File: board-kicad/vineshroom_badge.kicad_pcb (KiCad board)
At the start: 2 copper layers, 95 x 95.7 mm, 74 parts, among them IC1 ATTINY20-X, P1 CONN_01X05, Q1 Q_NMOS_DGS

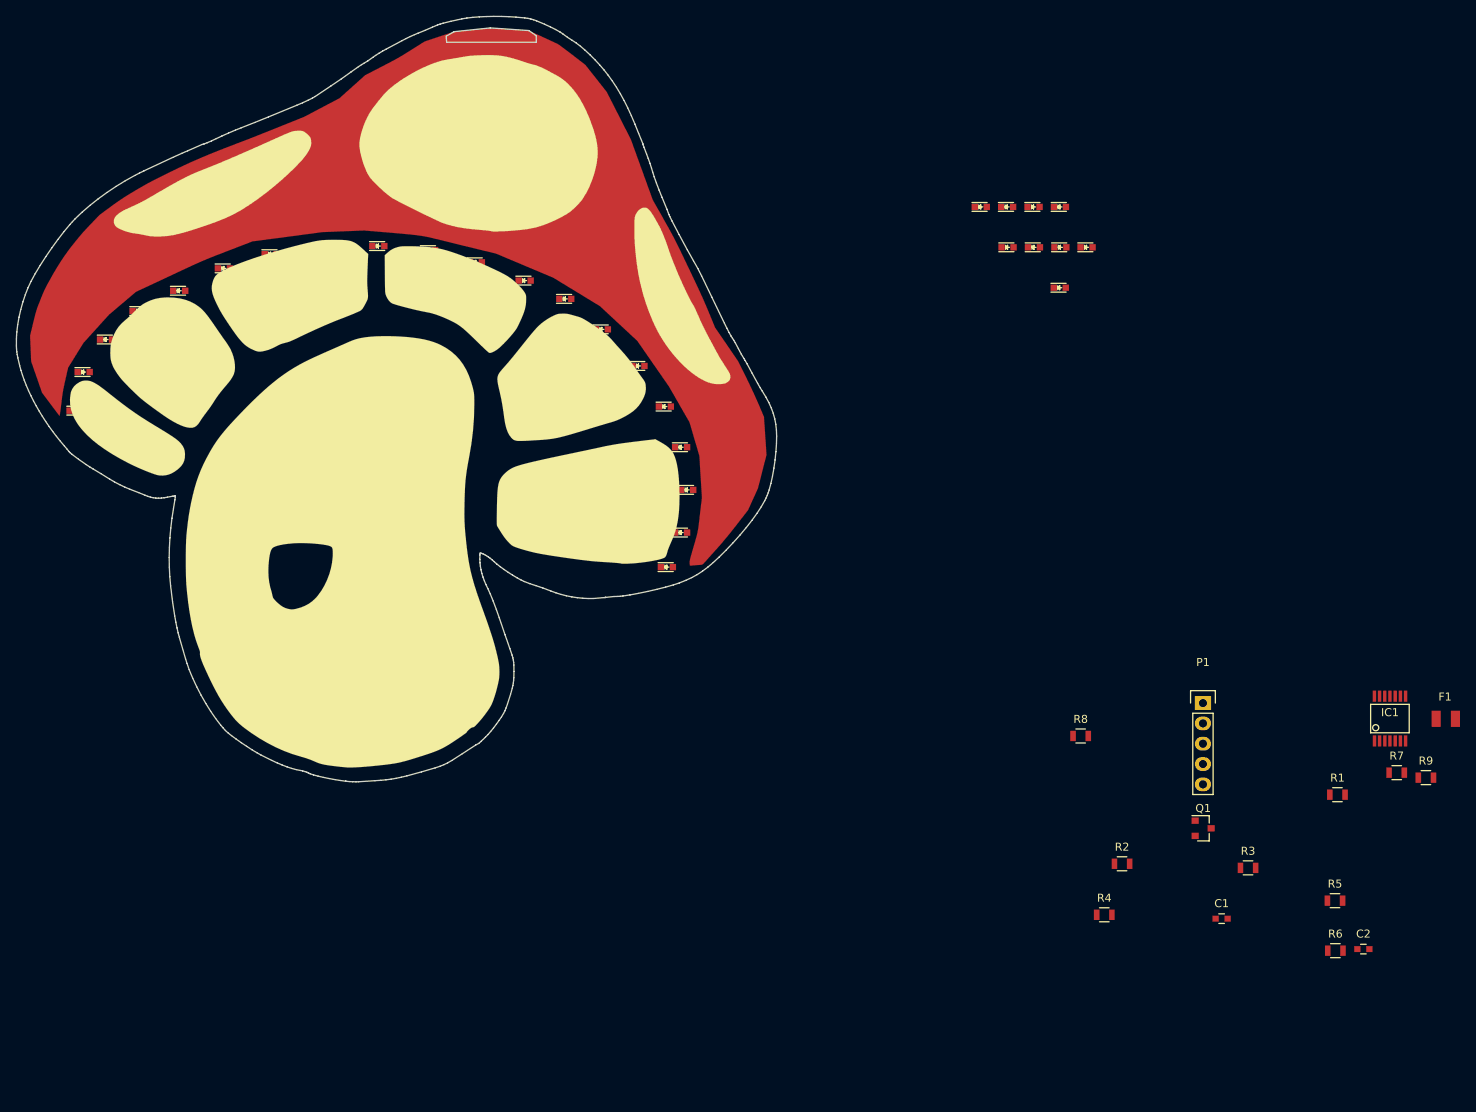
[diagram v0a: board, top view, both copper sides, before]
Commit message: starting LED placement
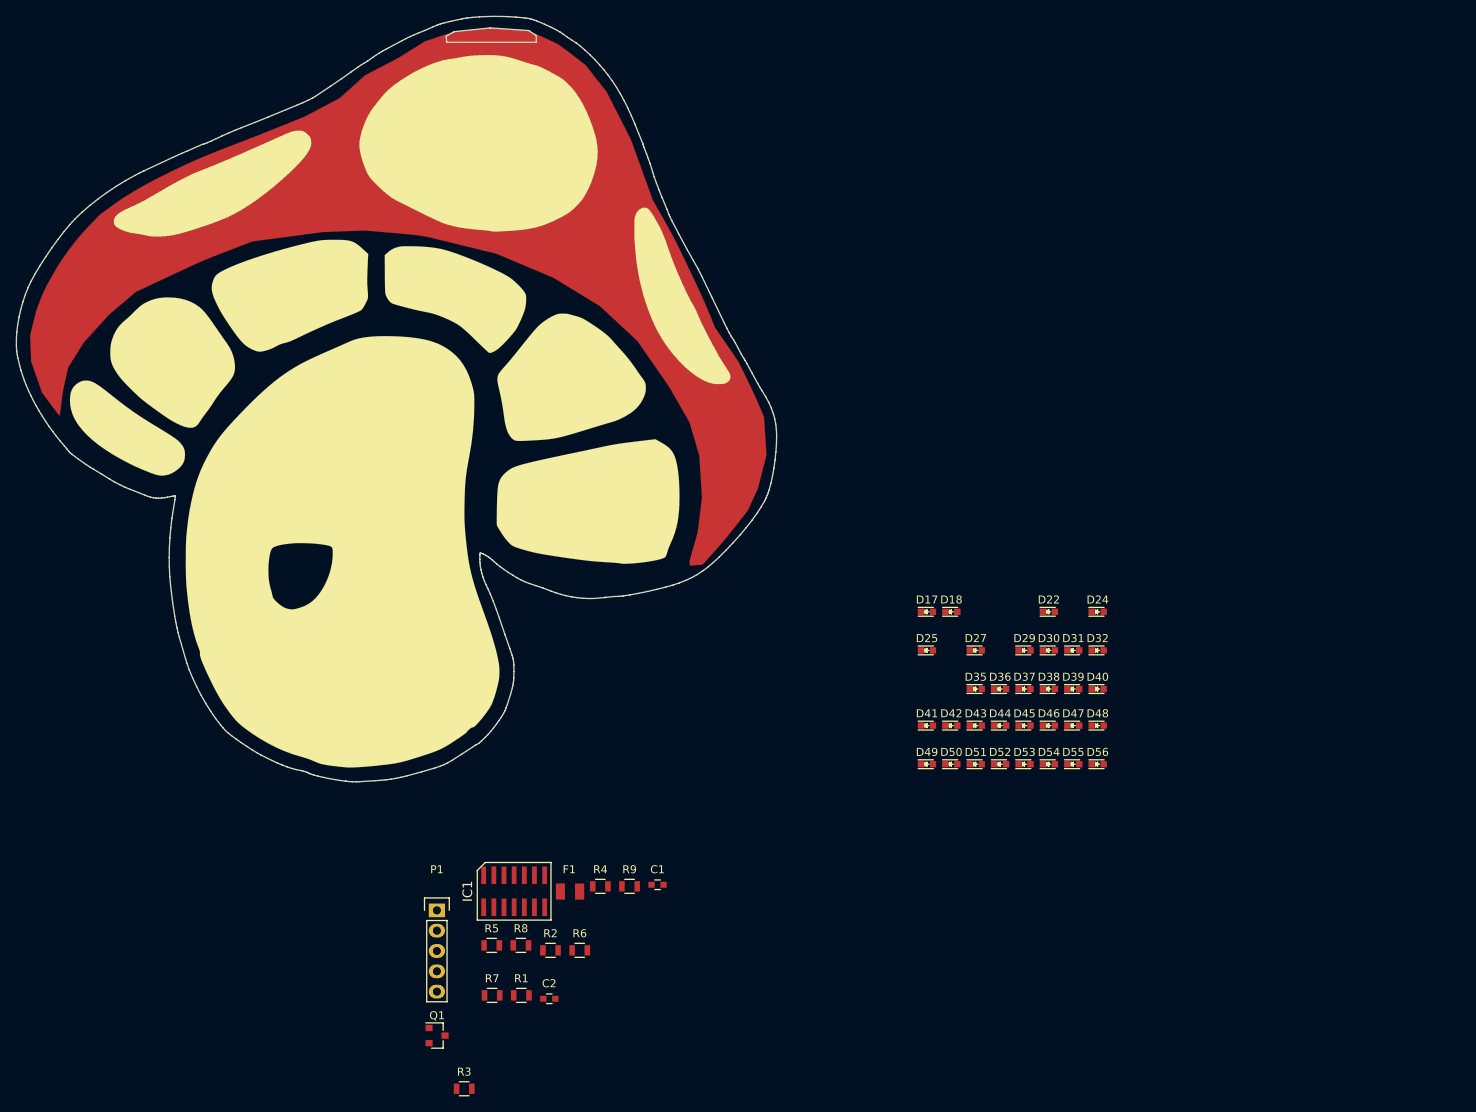
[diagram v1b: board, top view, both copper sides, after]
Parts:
- removed the G*** at (104.1, 75.7) (x3)
- added G*** (x2): LOGO, LOGO, F.Cu at (104.1, 75.7)
- added G***: LOGO, LOGO, F.Cu at (108.4, 160.3)
- IC1: footprint SMD_Packages:SSOP-14 -> spang_badge:ATTINY20_SOIC-14
- moved D48 134.2 mm to (193.3, 116.6)
- moved D24 125.6 mm to (193.3, 102.4)
- moved D22 124.2 mm to (187.2, 102.4)
- moved R7 116.5 mm to (117.6, 150.3)
- moved D55 113.5 mm to (190.2, 121.4)
- moved F1 111.6 mm to (127.3, 137.3)
- moved IC1 111.6 mm to (120.4, 137.3)
- moved D18 111.0 mm to (175.0, 102.4)
- moved D27 109.2 mm to (178.1, 107.2)
- moved D32 106.4 mm to (193.3, 107.2)
- moved R5 105.6 mm to (117.5, 144.1)
- moved R1 105.1 mm to (121.2, 150.3)
- moved D8 105.0 mm to (89.7, 80.8), turned to 90 degrees
- moved D53 102.8 mm to (184.2, 121.4)
- moved C2 101.9 mm to (124.7, 150.7)
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
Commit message: final touches on shroom badge
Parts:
- removed D53, D54, D55, D56: LED, LEDs:LED_0603
- removed the G*** at (104.1, 75.7) (x2)
- removed the G*** at (108.4, 160.3)
- removed P1: CONN_01X05, Pin_Headers:Pin_Header_Straight_1x05
- added BT1: Battery_Cell, vine_badge:COINCELL_20MM, B.Cu at (136.4, 127.9)
- added G***: LOGO, vine_badge:dousig10x10, F.Cu at (146.1, 98.0)
- added G***: LOGO, LOGO, F.Cu at (140.5, 94.1)
- added G***: LOGO, LOGO, F.Cu at (213.4, 100.7)
- added G***: LOGO, vine_badge:dousig10x10, B.Cu at (135.6, 112.6)
- added G***: LOGO, vine_badge:jergesig10x10, B.Cu at (170.4, 78.6)
- added G***: LOGO, vine_badge:GRANTSIG10X10, B.Cu at (110.6, 75.2)
- added G***: LOGO, vine_badge:tmg2020, B.Cu at (139.3, 86.3)
- added J1: CONN-TAGCONNECT-TC2050, vine_badge:TC2050_IDC, B.Cu at (163.6, 115.2)
- added R10: 1K, Resistors_SMD:R_0805, B.Cu at (145.3, 103.7)
- added SW1: SW_SPST, Buttons_Switches_SMD:SW_SPST_EVQPE1, B.Cu at (129.4, 84.8)
- C1, C2, F1, IC1, Q1, R1, R2, R3, R4, R5, R6, R7, R8: moved to B.Cu
- R9: value R -> 10K; moved to B.Cu
- moved D24 88.6 mm to (106.3, 85.4)
- moved D22 84.5 mm to (103.8, 88.4), turned to 180 degrees
- moved D30 79.2 mm to (112.6, 80.6), turned to 180 degrees
- moved D31 79.1 mm to (116.3, 78.9), turned to 180 degrees
- moved D32 78.8 mm to (120.3, 77.4), turned to 180 degrees
- moved D29 78.5 mm to (109.5, 82.8)
- moved R3 76.7 mm to (153.4, 96.2), turned to 270 degrees
- moved D39 74.8 mm to (124.6, 76.1)
- moved D40 74.4 mm to (128.8, 74.9), turned to 180 degrees
- moved D18 73.7 mm to (102.1, 91.6), turned to 180 degrees
- moved D17 70.7 mm to (101.6, 95.1)
- moved R1 65.4 mm to (158.0, 96.2), turned to 270 degrees
- moved C2 59.0 mm to (158.0, 101.9), turned to 90 degrees
- moved R2 57.5 mm to (155.7, 96.2), turned to 270 degrees
- moved R5 57.2 mm to (148.9, 96.2), turned to 270 degrees
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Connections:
- IC1 pad 2: /TPICLK/CTOUCH_I -> /TCK
- IC1 pad 3: /TPIDATA/CTOUCH_O -> /TDI
- IC1 pad 5: Net-(IC1-Pad5) -> /BTN
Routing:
- net GND: track 0.00 -> 243.8 mm, vias 0 -> 9
- net Net-(D10-Pad1): track 0.00 -> 189.0 mm, vias 0 -> 8
- net Net-(D10-Pad2): track 0.00 -> 150.4 mm, vias 0 -> 4
- net Net-(D1-Pad2): track 0.00 -> 143.9 mm, vias 0 -> 7
- net Net-(D13-Pad2): track 0.00 -> 143.2 mm, vias 0 -> 7
- net Net-(D12-Pad2): track 0.00 -> 137.2 mm, vias 0 -> 12
- net Net-(D14-Pad2): track 0.00 -> 135.8 mm, vias 0 -> 4
- net Net-(D1-Pad1): track 0.00 -> 105.0 mm, vias 0 -> 3
- net Net-(D11-Pad2): track 0.00 -> 103.8 mm, vias 0 -> 10
- net Net-(BT1-Pad1): track 0.00 -> 55.7 mm
- net /BTN: track 0.00 -> 50.7 mm, vias 0 -> 2
- net +BATT: track 0.00 -> 49.7 mm, vias 0 -> 3
- net Net-(BT1-Pad2): track 0.00 -> 33.3 mm
- net /TDI: track 0.00 -> 18.2 mm, vias 0 -> 2
- net /RST: track 0.00 -> 16.7 mm
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- added copper zone on B.Cu, net GND
- added copper zone on F.Cu, net GND
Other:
- net class Default: clearance 0.2 -> 0.2032
- rule trace_clearance: 0.2 -> 0.2032
- rule trace_min: 0.2 -> 0.2032
- rule via_min_drill: 0.3 -> 0.4
- rule via_min_size: 0.4 -> 0.6

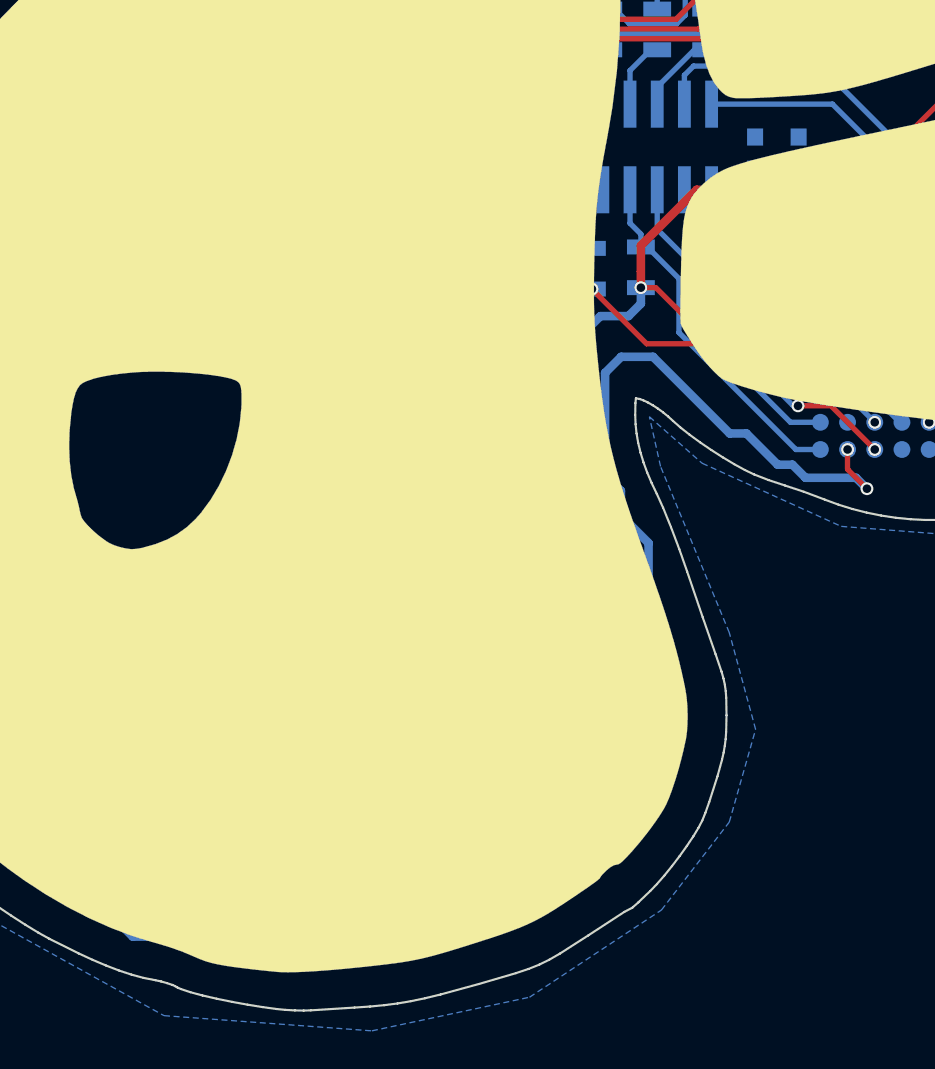
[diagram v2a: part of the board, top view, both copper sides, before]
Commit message: working on spang badge v2. TODO: fix B-CU
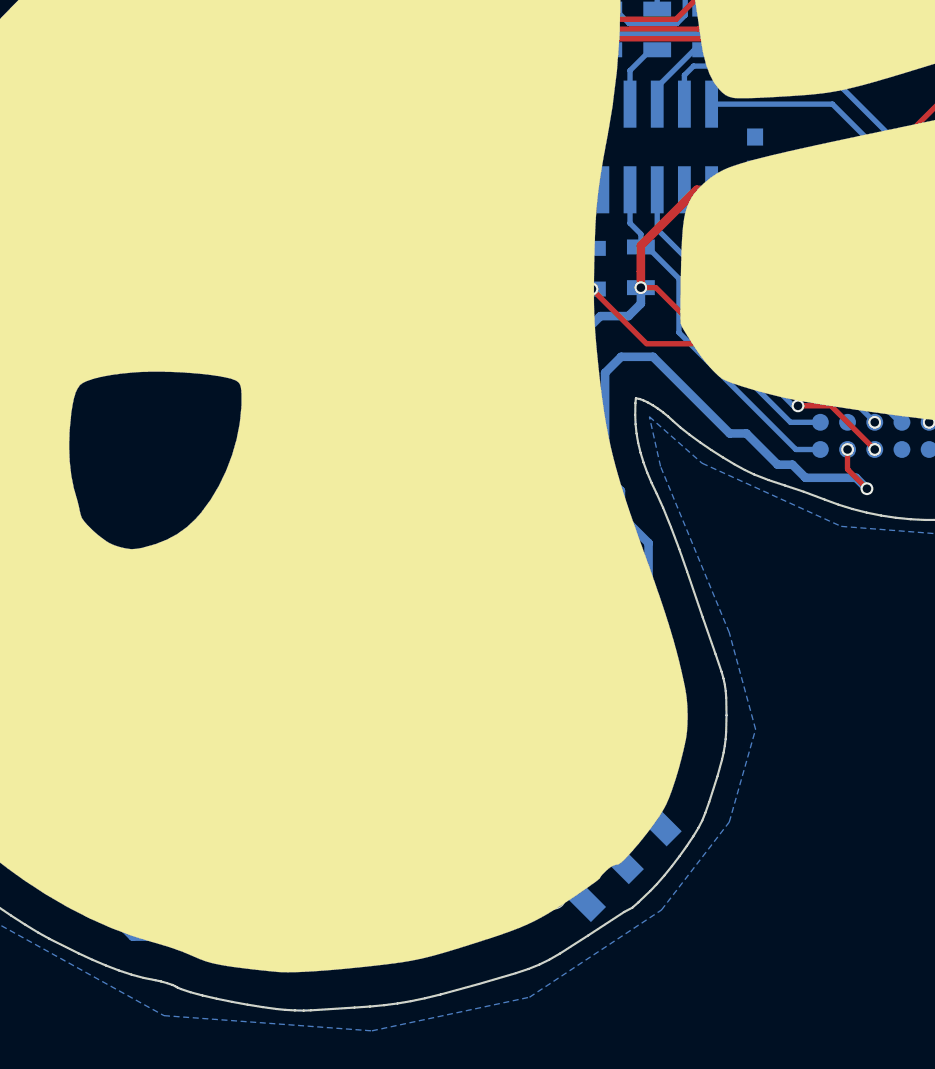
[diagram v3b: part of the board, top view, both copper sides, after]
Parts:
- added ON/OFF: SW_DPDT_x2, vine_badge:JS202011JAQN, B.Cu at (151.0, 134.3)
- C1: value C -> 100nF
- C2: value C -> 1uF
- R9: value 10K -> 1K
- moved C1 17.9 mm to (144.1, 110.2), turned to 180 degrees
- moved Q1 0.99 mm to (150.4, 122.0)
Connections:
- F1 pad 2: Net-(BT1-Pad1) -> Net-(F1-Pad2)
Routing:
- net Net-(F1-Pad2): track 0.00 -> 20.7 mm
- net Net-(BT1-Pad1): track 55.7 -> 43.4 mm
- net Net-(BT1-Pad2): track 33.3 -> 32.3 mm
- net +BATT: track 49.7 -> 50.7 mm
